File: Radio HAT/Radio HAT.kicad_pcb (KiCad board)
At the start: 4 copper layers, 65 x 45 mm, 29 parts, among them J1 Raspberry_Pi_2_3, J2 Coax SMA, J3 Barrel_Jack, J4 VCC, J5 6V, J6 GND, J7 V_RF, U1 RFM98PW, U2 AZ2185D-ADJTRG1

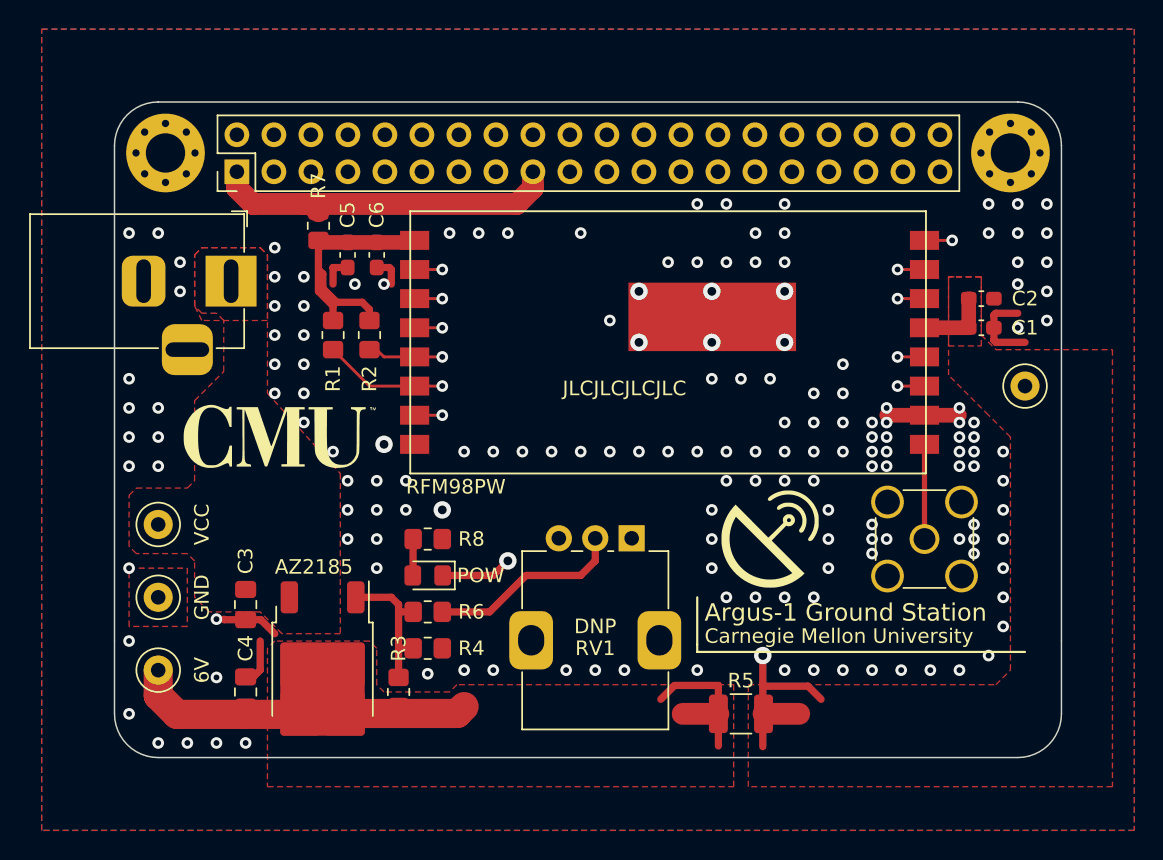
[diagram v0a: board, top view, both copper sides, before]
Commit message: Added gerbers, fixed silkscreen overlaps
Minor fixes to fix parts of silkscreen overlapping or crossing into footprints, generated gerber files for v1.1
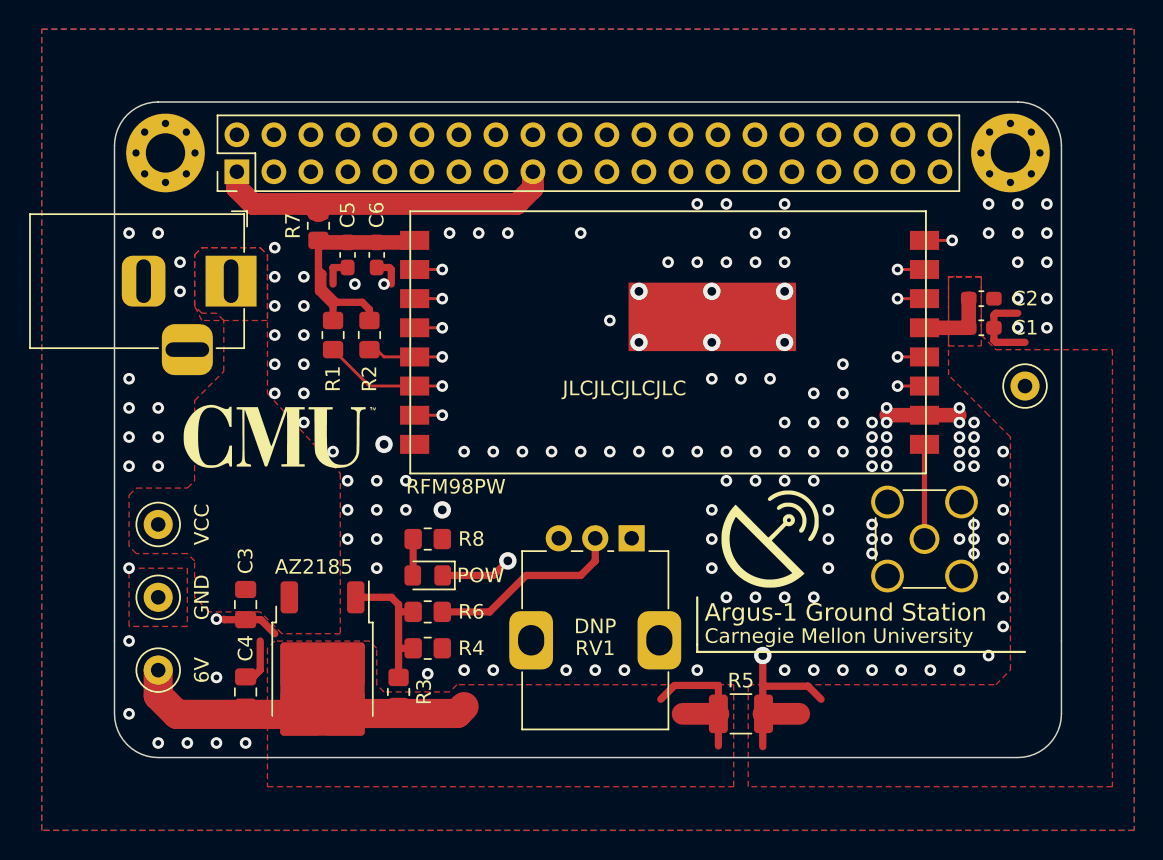
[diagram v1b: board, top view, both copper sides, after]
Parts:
- C1: value 0.1uF -> 0.1uF, 6.3V
- C2: value 10uF -> 10uF, 6.3V
- C3: value 10uF -> 10uF, 25V
- C4: value 22uF -> 22uF, 25V
- C5: value DNP -> DNP, 0.1uF, 10V
- C6: value DNP -> DNP, 10uF, 10V

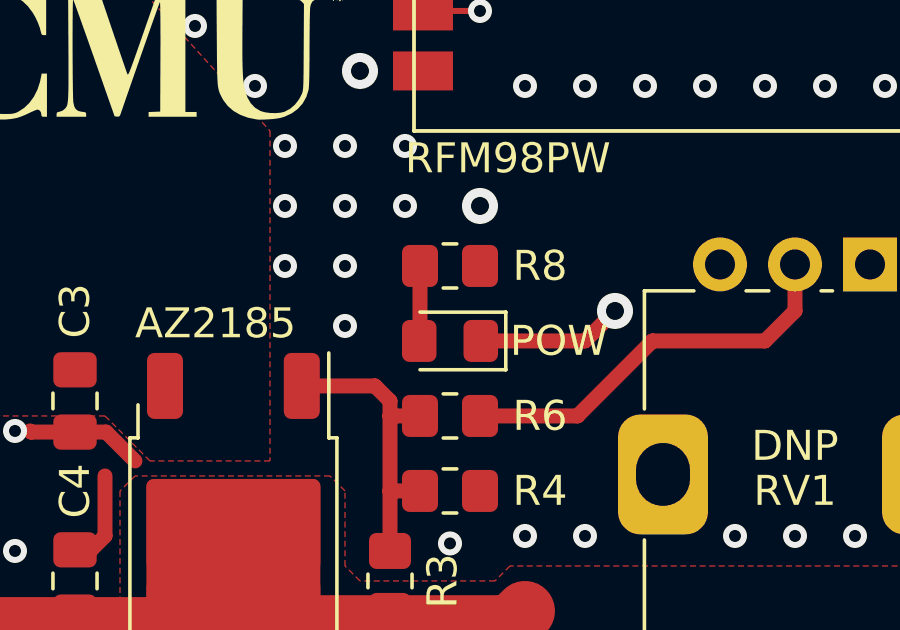
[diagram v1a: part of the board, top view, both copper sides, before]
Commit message: Fixed LED placement
LED was initially placed backwards
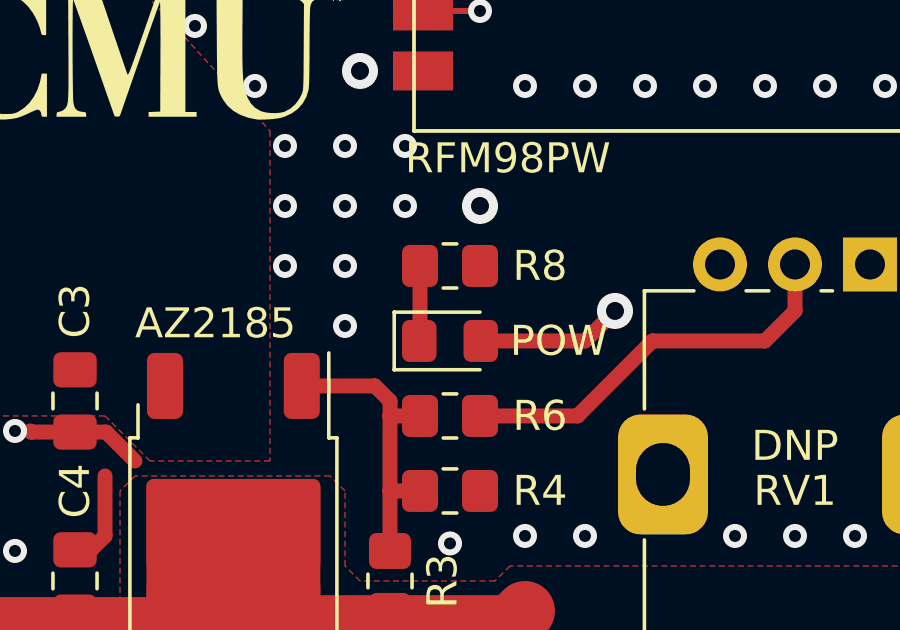
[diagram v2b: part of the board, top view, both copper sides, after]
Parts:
- turned D1 to 0 degrees
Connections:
- D1 pad 1: /V_RF -> Net-(D1-K)
- D1 pad 2: Net-(D1-A) -> /V_RF
- R8 pad 2: Net-(D1-A) -> Net-(D1-K)
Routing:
- net Net-(D1-K): track 0.00 -> 2.51 mm
- net Net-(D1-A): track 2.51 -> 0.00 mm
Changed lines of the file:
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@@
   (net 39 "unconnected-(RV1-Pad3)")
   (net 40 "/V_RF")
-  (net 41 "Net-(D1-A)")
+  (net 41 "Net-(D1-K)")
   (footprint "Resistor_SMD:R_0805_2012Metric_Pad1.20x1.40mm_HandSolder" (layer "F.Cu")
     (at 121.5 130 180)
@@
       (net 2 "GND") (pintype "passive"))
     (pad "2" smd roundrect (at 1 0 180) (size 1.2 1.4) (layers "F.Cu" "F.Paste" "F.Mask") (roundrect_rratio 0.2083333333)
-      (net 41 "Net-(D1-A)") (pintype "passive"))
+      (net 41 "Net-(D1-K)") (pintype "passive"))
     (model "${KICAD6_3DMODEL_DIR}/Resistor_SMD.3dshapes/R_0805_2012Metric.wrl"
       (offset (xyz 0 0 0))
@@
   )
   (footprint "LED_SMD:LED_0805_2012Metric_Pad1.15x1.40mm_HandSolder" (layer "F.Cu")
-    (at 121.5 132.5 180)
+    (at 121.5 132.5)
     (descr "LED SMD 0805 (2012 Metric), square (rectangular) end terminal, IPC_7351 nominal, (Body size source: https://docs.google.com/spreadsheets/d/1BsfQQcO9C6DZCsRaXUlFlo91Tg2WpOkGARC1WS5S8t0/edit?usp=sharing), generated with kicad-footprint-generator")
     (tags "LED handsolder")
@@
     (fp_line (start 1 0.6) (end 1 -0.6)
       (stroke (width 0.1) (type solid)) (layer "F.Fab"))
-    (pad "1" smd roundrect (at -1.025 0 180) (size 1.15 1.4) (layers "F.Cu" "F.Paste" "F.Mask") (roundrect_rratio 0.2173913043)
-      (net 40 "/V_RF") (pinfunction "K") (pintype "passive"))
-    (pad "2" smd roundrect (at 1.025 0 180) (size 1.15 1.4) (layers "F.Cu" "F.Paste" "F.Mask") (roundrect_rratio 0.2173913043)
-      (net 41 "Net-(D1-A)") (pinfunction "A") (pintype "passive"))
+    (pad "1" smd roundrect (at -1.025 0) (size 1.15 1.4) (layers "F.Cu" "F.Paste" "F.Mask") (roundrect_rratio 0.2173913043)
+      (net 41 "Net-(D1-K)") (pinfunction "K") (pintype "passive"))
+    (pad "2" smd roundrect (at 1.025 0) (size 1.15 1.4) (layers "F.Cu" "F.Paste" "F.Mask") (roundrect_rratio 0.2173913043)
+      (net 40 "/V_RF") (pinfunction "A") (pintype "passive"))
     (model "${KICAD6_3DMODEL_DIR}/LED_SMD.3dshapes/LED_0805_2012Metric.wrl"
       (offset (xyz 0 0 0))
@@
   (segment (start 127 128) (end 127 131.5) (width 0.5) (layer "In2.Cu") (net 40))
   (segment (start 145 128.5) (end 143.5 127) (width 0.5) (layer "In2.Cu") (net 40))
-  (segment (start 120.475 132.5) (end 120.5 132.475) (width 0.5) (layer "F.Cu") (net 41))
-  (segment (start 120.5 132.475) (end 120.5 130) (width 0.5) (layer "F.Cu") (net 41))
+  (segment (start 120.5 132.475) (end 120.475 132.5) (width 0.35925) (layer "F.Cu") (net 41))
+  (segment (start 120.5 130) (end 120.5 132.475) (width 0.5) (layer "F.Cu") (net 41))
   (zone (net 1) (net_name "+6V") (layer "F.Cu") (hatch edge 0.5)
     (priority 3)

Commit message: Updated BOM, removed gerbers
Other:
- board text removed: "JLCJLCJLCJLC"
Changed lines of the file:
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@@
-    (effects (font (size 1 1) (thickness 0.15)) (justify left bottom))
-  )
-  (gr_text "JLCJLCJLCJLC" (at 130.75 120.25) (layer "F.SilkS")
     (effects (font (size 1 1) (thickness 0.15)) (justify left bottom))
   )
